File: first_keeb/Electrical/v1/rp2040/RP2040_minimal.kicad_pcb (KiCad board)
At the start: 4 copper layers, 67.1 x 66.8 mm, 78 parts, among them J1 Conn_01x04_Socket, P1 USB-TYPE-C-016, Q1 BSS138, SW1 TS-1187A-B-A-B, SW2 TS-1187A-B-A-B, SW3 BUTT1, SW4 BUTT3, SW5 BUTT2, U1 PRTR5V0U2X, U2 ME6208A44M3G, U3 RP2040, U4 ME6212C25M5G, U5 W25Q16JVSS, U6 ME6212C33M5G, U7 SLSS49E, U8 SLSS49E, U9 SLSS49E, Y1 12MHz

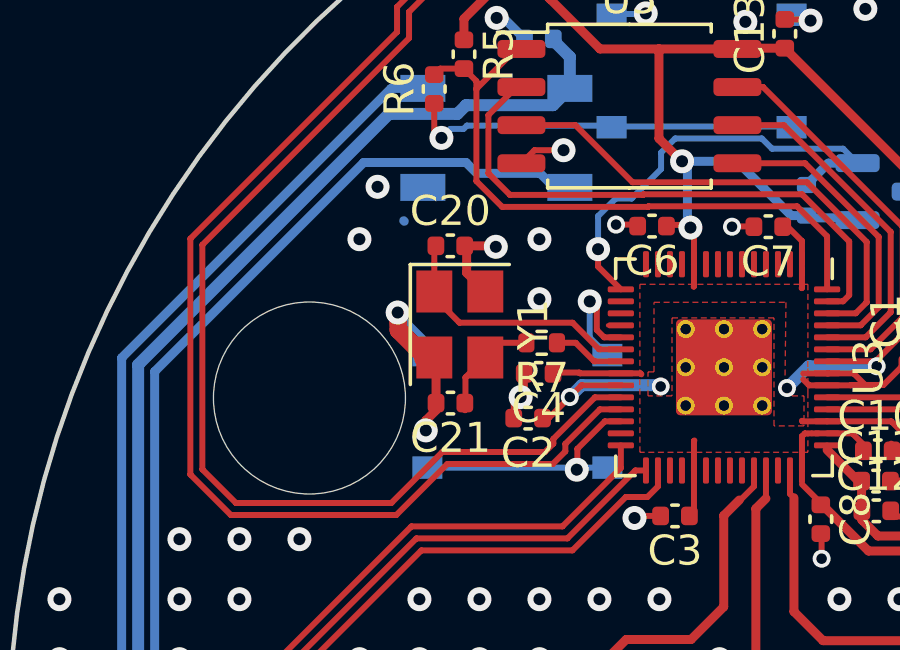
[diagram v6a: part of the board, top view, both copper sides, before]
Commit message: changes caps to match 12MHz crystal
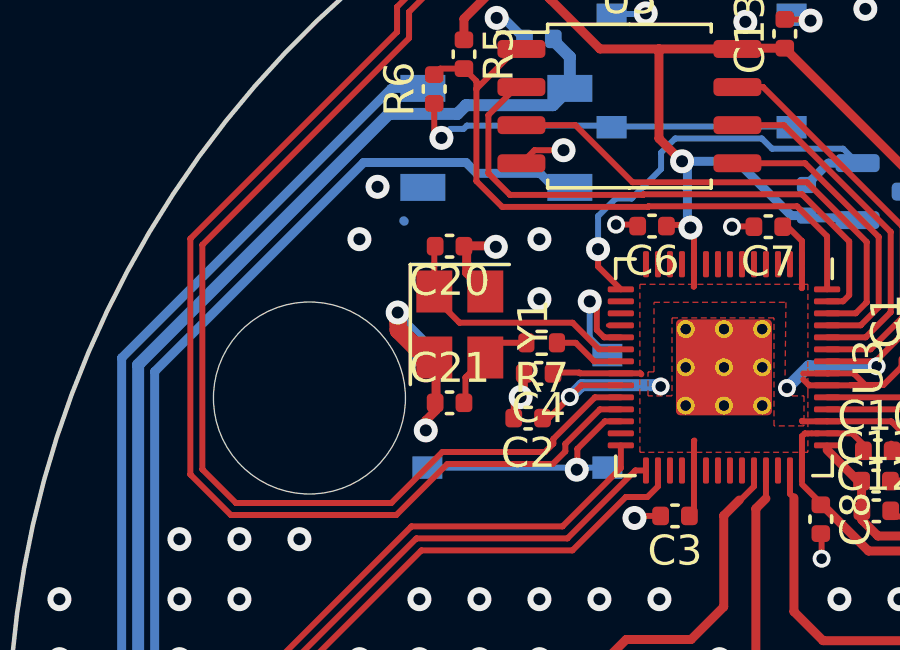
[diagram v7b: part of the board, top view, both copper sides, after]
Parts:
- turned C21 to 0 degrees
- turned C20 to 180 degrees
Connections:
- C20 pad 1: OSC_IN -> GND
- C20 pad 2: GND -> OSC_IN
- C21 pad 1: Net-(C21-Pad1) -> GND
- C21 pad 2: GND -> Net-(C21-Pad2)
- R7 pad 2: Net-(C21-Pad1) -> Net-(C21-Pad2)
- Y1 pad 3: Net-(C21-Pad1) -> Net-(C21-Pad2)
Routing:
- net Net-(C21-Pad1): track 4.52 -> 0.00 mm
- net Net-(C21-Pad2): track 0.00 -> 4.28 mm

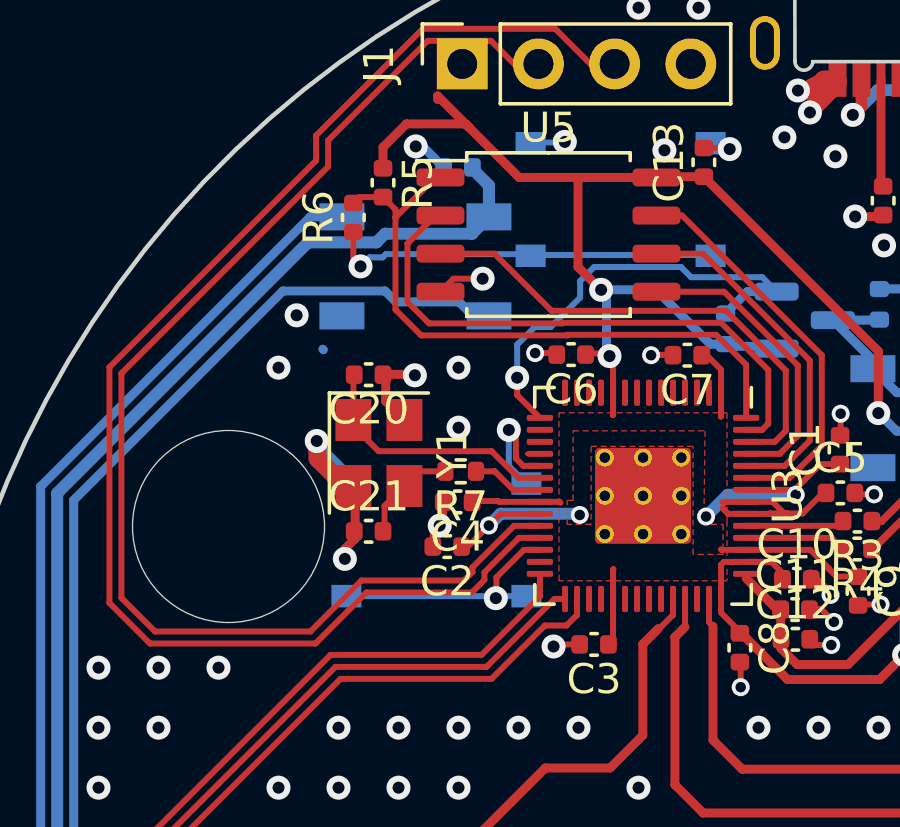
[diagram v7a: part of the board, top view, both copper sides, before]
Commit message: adds pullup for run pin
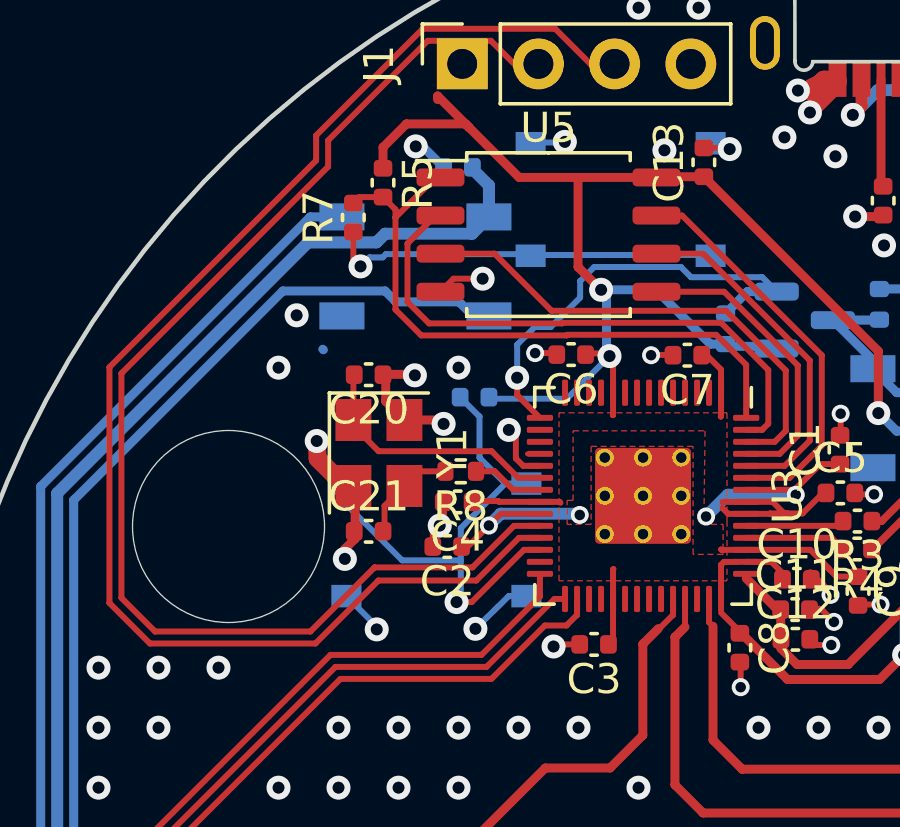
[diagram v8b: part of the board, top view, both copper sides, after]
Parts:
- added R6: 1k, Capacitor_SMD:C_0402_1005Metric, B.Cu at (84.7, 83.7)
- turned SW2 to 0 degrees
- renumbered R9 to R10, R6 to R7, R7 to R8, R8 to R9
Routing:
- net Net-(U3-RUN): track 8.59 -> 17.8 mm
- net +3V3: track 80.7 -> 85.4 mm
- net GND: track 90.5 -> 92.1 mm, vias 313 -> 315
